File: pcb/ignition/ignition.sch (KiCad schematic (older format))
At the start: 174 parts, among them IC1 LTC4151, IC2 LTC4151, IC3 LTC4151, IC4 LTC4151, IC5 LTC4151, IC6 LTC4151, IC7 ADP3335, IC8 STM32F437VIT6, J1 PSU, J10 CH2, J11 CH4, J12 ARM, J13 UART1, J14 UART2, J15 CH1, J16 CH3, J17 CH5, J2 LED1, J3 PSU, J4 LED2, J5 5v In, J6 5v Out, J7 LED3, J8 LED4, J9 LED5, K1 16A SPST, K2 16A SPST, K3 16A SPST, K4 16A SPST, K5 16A SPST, K6 16A SPST, P1 SWD_TC, Q1 NFET, Q2 NFET, Q3 NFET, Q4 NFET, Q5 NFET, Q6 NFET, U1 MICROSD, X1 Molex Wire, X10 GRN LED, X11 LED Bezel, X12 24V PSU, X13 5V PSU, X14 GRN LED, X15 LED Bezel, X16 Molex Wire, X17 M12 Socket, X18 M12 Plug, X19 Molex Wire, X2 GRN LED, X20 M12 Socket, X21 M12 Plug, X22 Bi-LED, X23 LED Bezel, X24 Molex Wire, X25 M12 Socket, X26 M12 Plug, X27 Molex Wire, X28 M12 Socket, X29 M12 Plug, X3 LED Bezel, X30 Molex Wire, X31 M12 Socket, X32 M12 Plug, X33 Hole, X34 Hole, X35 Hole, X36 Hole, X4 GRN LED, X5 LED Bezel, X6 GRN LED, X7 LED Bezel, X8 Key Switch, X9 AC Input, Y1 26M

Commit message: ignition pcb almost complete
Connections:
- net ARM_GRN: now also IC8.51 (PB12); no longer IC8.39 (PE8)
- net ARM_RED: now also IC8.52 (PB13); no longer IC8.40 (PE9)
- net ARM_SUPPLY: now also IC8.1 (PE2); no longer IC8.55 (PD8)
- net CH1_FIRE: now also IC8.36 (PB1); no longer IC8.56 (PD9)
- net CH2_FIRE: now also IC8.37 (PB2); no longer IC8.57 (PD10)
- net CH3_FIRE: now also IC8.38 (PE7); no longer IC8.58 (PD11)
- net CH4_FIRE: now also IC8.39 (PE8); no longer IC8.59 (PD12)
- net CH5_FIRE: now also IC8.40 (PE9); no longer IC8.60 (PD13)
- net FIRE_DIST: now also D1.1, D2.1, D6.1, D7.1, D8.1, K1.2, K2.2, K4.2, K5.2, K6.2
- net PSU_MON: now also IC8.24 (PA1); no longer IC8.34 (PC5)
- net STATUS: now also IC8.64 (PC7); no longer IC8.43 (PE12)
- net VCC: now also D3.1, K3.2
- net at IC3.10 (SENSE-), K3.3, R13.1: no longer D3.1, K3.2
- net at IC4.10 (SENSE-), K4.3, R31.1: no longer D6.1, K4.2
- net at IC1.10 (SENSE-), K1.3, R7.1: no longer D1.1, K1.2
- net at IC5.10 (SENSE-), K5.3, R32.1: no longer D7.1, K5.2
- net at IC2.10 (SENSE-), K2.3, R8.1: no longer D2.1, K2.2
- net at IC6.10 (SENSE-), K6.3, R33.1: no longer D8.1, K6.2
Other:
- note added: "ADC12 IN 10-14"
- note removed: "ADC12 IN 10-15"
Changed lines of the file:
@@
 	1    0    0    -1
 $EndComp
-Wire Wire Line
-	3625 2600 3325 2600
 Connection ~ 2925 2600
 Wire Wire Line
 	3325 2750 3325 2850
 Wire Wire Line
-	3325 2750 3325 2600
-Connection ~ 3325 2750
-Connection ~ 3325 2600
-Wire Wire Line
-	3325 2600 2925 2600
-Wire Wire Line
 	1425 3675 1425 3400
 Connection ~ 1425 3400
@@
 Channel 1:
 Wire Wire Line
-	7975 2675 7975 2525
-Connection ~ 7975 2675
-Connection ~ 7975 2525
-Wire Wire Line
-	7975 2525 8275 2525
-Wire Wire Line
-	7600 2525 7975 2525
-Wire Wire Line
 	6100 2525 7300 2525
 Wire Wire Line
@@
 Channel 2:
 Wire Wire Line
-	3025 5225 3025 5075
-Connection ~ 3025 5225
-Connection ~ 3025 5075
-Wire Wire Line
-	3025 5075 3325 5075
-Wire Wire Line
-	2650 5075 3025 5075
-Wire Wire Line
 	1150 5075 2350 5075
 Wire Wire Line
@@
 Channel 3:
 Wire Wire Line
-	7975 5225 7975 5075
-Connection ~ 7975 5225
-Connection ~ 7975 5075
-Wire Wire Line
-	7975 5075 8275 5075
-Wire Wire Line
-	7600 5075 7975 5075
-Wire Wire Line
 	6100 5075 7300 5075
 Wire Wire Line
@@
 Channel 4:
 Wire Wire Line
-	3025 7725 3025 7575
-Connection ~ 3025 7725
-Connection ~ 3025 7575
-Wire Wire Line
-	3025 7575 3325 7575
-Wire Wire Line
-	2650 7575 3025 7575
-Wire Wire Line
 	1150 7575 2350 7575
 Wire Wire Line
@@
 Channel 5:
 Wire Wire Line
-	7975 7725 7975 7575
-Connection ~ 7975 7725
-Connection ~ 7975 7575
-Wire Wire Line
-	7975 7575 8275 7575
-Wire Wire Line
-	7600 7575 7975 7575
-Wire Wire Line
 	6100 7575 7300 7575
 Wire Wire Line
@@
 Wire Wire Line
 	2025 1075 2075 1075
-Text Label 14125 5725 0    50   ~ 0
+Text Label 12725 6825 2    50   ~ 0
 ARM_GRN
-Text Label 14125 5825 0    50   ~ 0
+Text Label 12725 6925 2    50   ~ 0
 ARM_RED
 Text Label 14125 1225 0    50   ~ 0
@@
 Text Label 14125 1325 0    50   ~ 0
 CH2_CONT
-Text Label 14125 1725 0    50   ~ 0
+Text Label 12725 3825 2    50   ~ 0
 PSU_MON
-Text Label 14125 3925 0    50   ~ 0
+Text Label 14125 5025 0    50   ~ 0
 ARM_SUPPLY
-Text Label 14125 4125 0    50   ~ 0
+Text Label 12725 5725 2    50   ~ 0
 CH2_FIRE
-Text Label 14125 4025 0    50   ~ 0
+Text Label 12725 5625 2    50   ~ 0
 CH1_FIRE
-Text Label 14125 4225 0    50   ~ 0
+Text Label 14125 5525 0    50   ~ 0
 CH3_FIRE
-Text Label 14125 4325 0    50   ~ 0
+Text Label 14125 5725 0    50   ~ 0
 CH4_FIRE
-Text Label 14125 4425 0    50   ~ 0
+Text Label 14125 5825 0    50   ~ 0
 CH5_FIRE
 Text Label 12725 6725 2    50   ~ 0
@@
 	1    0    0    -1
 $EndComp
-Text Label 14125 6125 0    50   ~ 0
+Text Label 14125 1925 0    50   ~ 0
 STATUS
 $Comp
@@
 	14025 1625 14125 1625
 Wire Wire Line
-	14025 1725 14125 1725
+	12825 3825 12725 3825
 NoConn ~ 14025 1825
-NoConn ~ 14025 1925
 Text Notes 14700 1450 0    50   ~ 0
-ADC12 IN 10-15
+ADC12 IN 10-14
 Wire Wire Line
 	12725 6425 12825 6425
@@
 USART2_RX
 Wire Wire Line
-	14025 3925 14125 3925
+	14025 5025 14125 5025
 Wire Wire Line
-	14125 4025 14025 4025
+	12725 5625 12825 5625
 Wire Wire Line
-	14025 4125 14125 4125
+	12825 5725 12725 5725
 Wire Wire Line
-	14025 4225 14125 4225
+	14025 5525 14125 5525
 Wire Wire Line
-	14025 4325 14125 4325
+	14025 5725 14125 5725
 Wire Wire Line
-	14025 4425 14125 4425
+	14025 5825 14125 5825
 Wire Wire Line
-	14025 5725 14125 5725
+	12825 6825 12725 6825
 Wire Wire Line
-	14125 5825 14025 5825
+	12725 6925 12825 6925
 Wire Wire Line
-	14025 6125 14125 6125
+	14025 1925 14125 1925
 NoConn ~ 14025 6425
 NoConn ~ 14025 6325
 NoConn ~ 14025 6225
 NoConn ~ 14025 6025
-NoConn ~ 14025 5925
-NoConn ~ 14025 5525
 NoConn ~ 14025 5425
 NoConn ~ 14025 5325
 NoConn ~ 14025 5225
 NoConn ~ 14025 5125
-NoConn ~ 14025 5025
 NoConn ~ 14025 4925
 NoConn ~ 14025 4825
@@
 NoConn ~ 12825 7125
 NoConn ~ 12825 7025
-NoConn ~ 12825 6925
-NoConn ~ 12825 6825
 NoConn ~ 12825 6225
 NoConn ~ 12825 6125
-NoConn ~ 12825 5525
-NoConn ~ 12825 5625
-NoConn ~ 12825 5725
 NoConn ~ 12825 5825
 NoConn ~ 12825 5925
@@
 NoConn ~ 12825 4225
 NoConn ~ 12825 4125
-NoConn ~ 12825 3825
 NoConn ~ 12825 3725
 NoConn ~ 14025 3725
@@
 	1    0    0    -1
 $EndComp
+Text Label 7975 2675 2    50   ~ 0
+FIRE_DIST
+Wire Wire Line
+	7600 2525 8275 2525
+Text Label 7975 5225 2    50   ~ 0
+FIRE_DIST
+Wire Wire Line
+	7600 5075 8275 5075
+Text Label 3025 5225 2    50   ~ 0
+FIRE_DIST
+Wire Wire Line
+	2650 5075 3325 5075
+Text Label 3025 7725 2    50   ~ 0
+FIRE_DIST
+Wire Wire Line
+	2650 7575 3325 7575
+Text Label 7975 7725 2    50   ~ 0
+FIRE_DIST
+Wire Wire Line
+	7600 7575 8275 7575
+NoConn ~ 12825 5525
+NoConn ~ 14025 4025
+NoConn ~ 14025 4125
+NoConn ~ 14025 4225
+NoConn ~ 14025 4325
+NoConn ~ 14025 4425
+NoConn ~ 14025 6125
+NoConn ~ 14025 3925
+NoConn ~ 14025 5925
+NoConn ~ 14025 1725
+$Comp
+L voltages:24v #PWR?
+U 1 1 5CA17557
+P 3250 2750
+F 0 "#PWR?" H 3250 2860 50  0001 L CNN
+F 1 "24v" H 3250 2850 50  0000 C CNN
+F 2 "" H 3250 2750 50  0001 C CNN
+F 3 "" H 3250 2750 50  0001 C CNN
+	1    3250 2750
+	0    -1   -1   0
+$EndComp
+Wire Wire Line
+	2925 2600 3625 2600
+Wire Wire Line
+	3250 2750 3325 2750
+Connection ~ 3325 2750
 $EndSCHEMATC

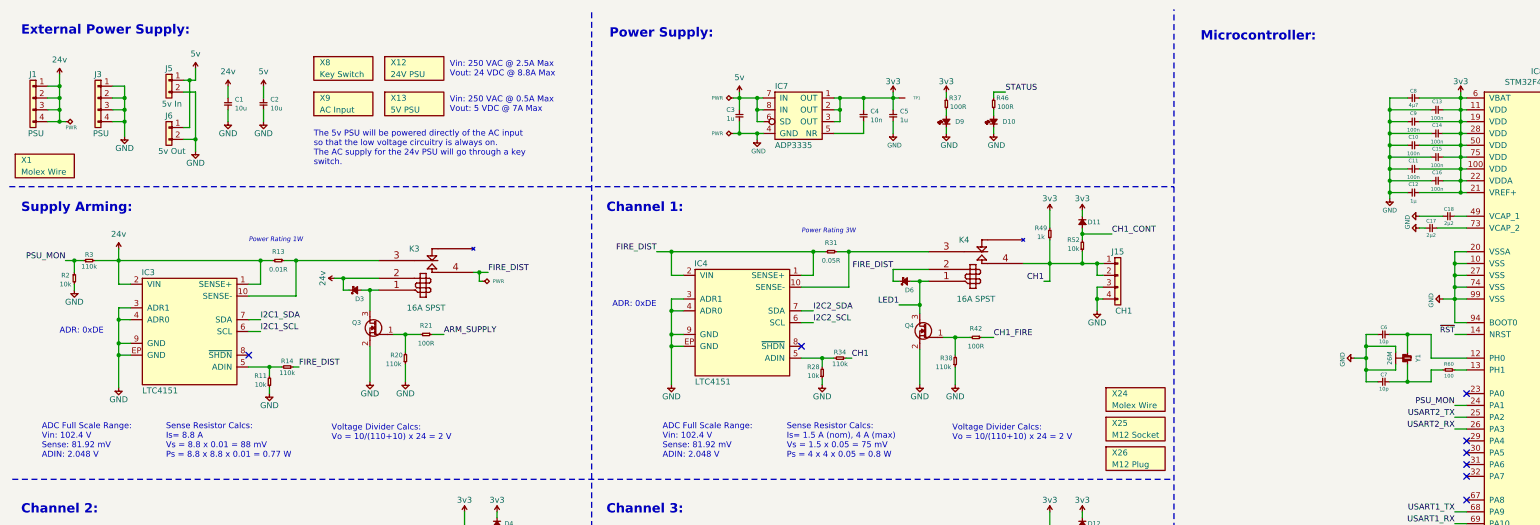
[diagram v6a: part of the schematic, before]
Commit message: finalised schematic and pcb copper, adding silk
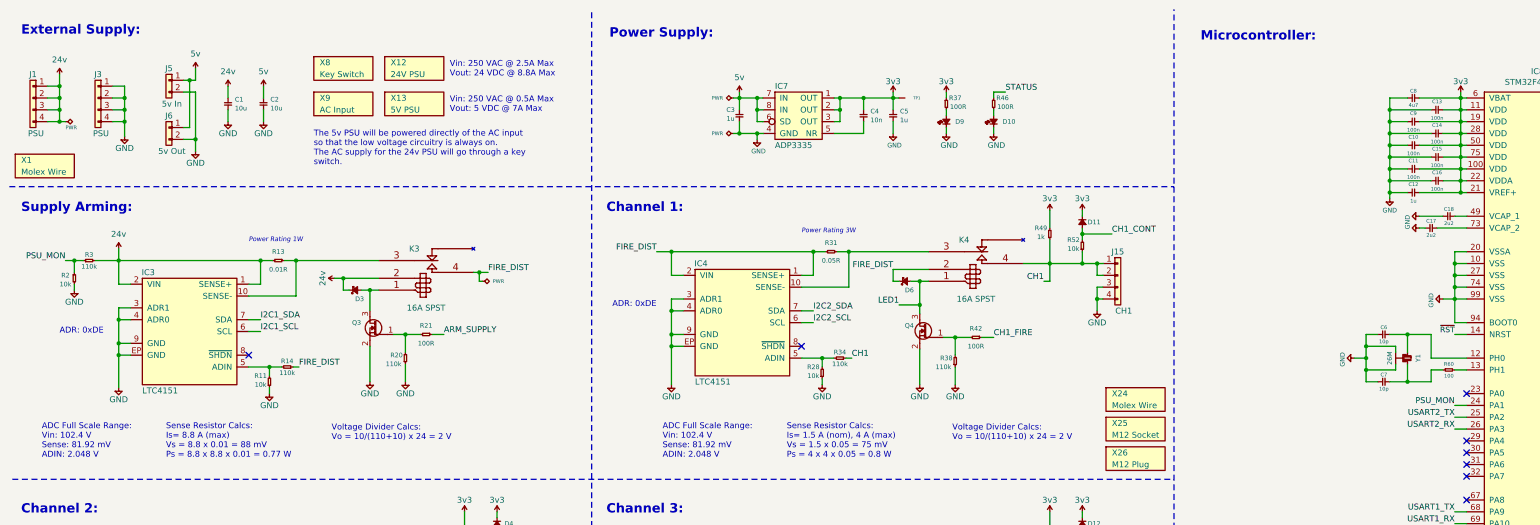
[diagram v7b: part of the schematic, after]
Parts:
- C12: value 1µ -> 1u
- C17, C18: value 2µ2 -> 2u2
- C8: value 4µ7 -> 4u7
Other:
- note added: "External Supply:"
- note added: "Sense Resistor Calcs:\nIs= 8.8 A (max)\nVs = 8.8 x 0.01 = 88 mV\nPs = 8.8 x 8.8 x 0.01 = 0.77 W"
- note removed: "External Power Supply:"
- note removed: "Sense Resistor Calcs:\nIs= 8.8 A\nVs = 8.8 x 0.01 = 88 mV\nPs = 8.8 x 8.8 x 0.01 = 0.77 W"
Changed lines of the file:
@@
 encoding utf-8
 Sheet 1 1
-Title "Valve Controller"
-Date "2018-11-03"
+Title "Ignition Board"
+Date "2018-11-11"
 Rev "1"
-Comp "Matt Coates"
-Comment1 ""
+Comp "Matthew Coates"
+Comment1 "Hybrid Ignition Controller"
 Comment2 ""
 Comment3 ""
@@
 $EndComp
 Text Notes 600  700  0    79   ~ 16
-External Power Supply:
+External Supply:
 Wire Wire Line
 	1425 2800 1525 2800
@@
 Power Rating 1W
 Text Notes 1825 4275 0    50   ~ 0
-Sense Resistor Calcs:\nIs= 8.8 A\nVs = 8.8 x 0.01 = 88 mV\nPs = 8.8 x 8.8 x 0.01 = 0.77 W
+Sense Resistor Calcs:\nIs= 8.8 A (max)\nVs = 8.8 x 0.01 = 88 mV\nPs = 8.8 x 8.8 x 0.01 = 0.77 W
 Text Notes 3225 4125 0    50   ~ 0
 Voltage Divider Calcs:\nVo = 10/(110+10) x 24 = 2 V
@@
 P 12725 2225
 F 0 "C18" H 12775 2165 31  0000 C CNN
-F 1 "2µ2" H 12775 2285 31  0000 C CNN
+F 1 "2u2" H 12775 2285 31  0000 C CNN
 F 2 "agg:0402" H 12725 2225 50  0001 C CNN
 F 3 "" H 12725 2225 50  0001 C CNN
@@
 P 12575 2325
 F 0 "C17" H 12625 2265 31  0000 C CNN
-F 1 "2µ2" H 12625 2385 31  0000 C CNN
+F 1 "2u2" H 12625 2385 31  0000 C CNN
 F 2 "agg:0402" H 12575 2325 50  0001 C CNN
 F 3 "" H 12575 2325 50  0001 C CNN
@@
 P 12325 2025
 F 0 "C12" H 12375 2095 31  0000 C CNN
-F 1 "1µ" H 12375 1955 31  0000 C CNN
+F 1 "1u" H 12375 1955 31  0000 C CNN
 F 2 "agg:0402" H 12325 2025 50  0001 C CNN
 F 3 "" H 12325 2025 50  0001 C CNN
@@
 P 12325 1225
 F 0 "C8" H 12375 1285 31  0000 C CNN
-F 1 "4µ7" H 12375 1165 31  0000 C CNN
+F 1 "4u7" H 12375 1165 31  0000 C CNN
 F 2 "agg:0402" H 12325 1225 50  0001 C CNN
 F 3 "" H 12325 1225 50  0001 C CNN
@@
 NoConn ~ 14025 1725
 $Comp
-L voltages:24v #PWR?
+L voltages:24v #PWR0101
 U 1 1 5CA17557
 P 3250 2750
-F 0 "#PWR?" H 3250 2860 50  0001 L CNN
+F 0 "#PWR0101" H 3250 2860 50  0001 L CNN
 F 1 "24v" H 3250 2850 50  0000 C CNN
 F 2 "" H 3250 2750 50  0001 C CNN

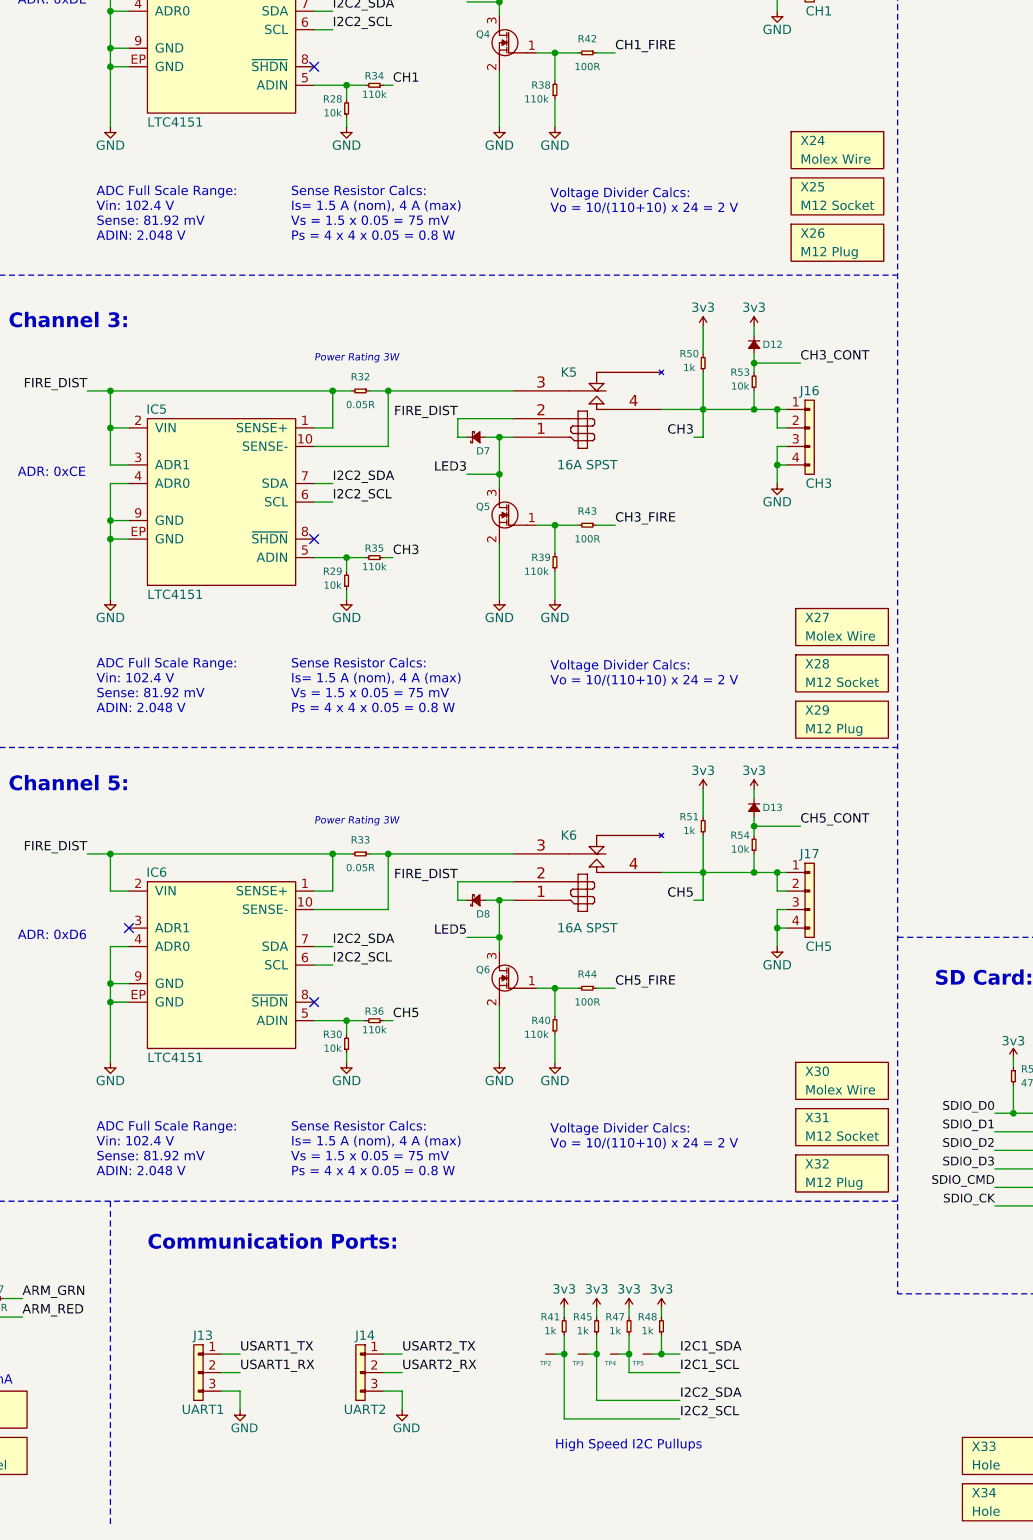
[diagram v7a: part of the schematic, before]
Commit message: made changes to ignition as per review
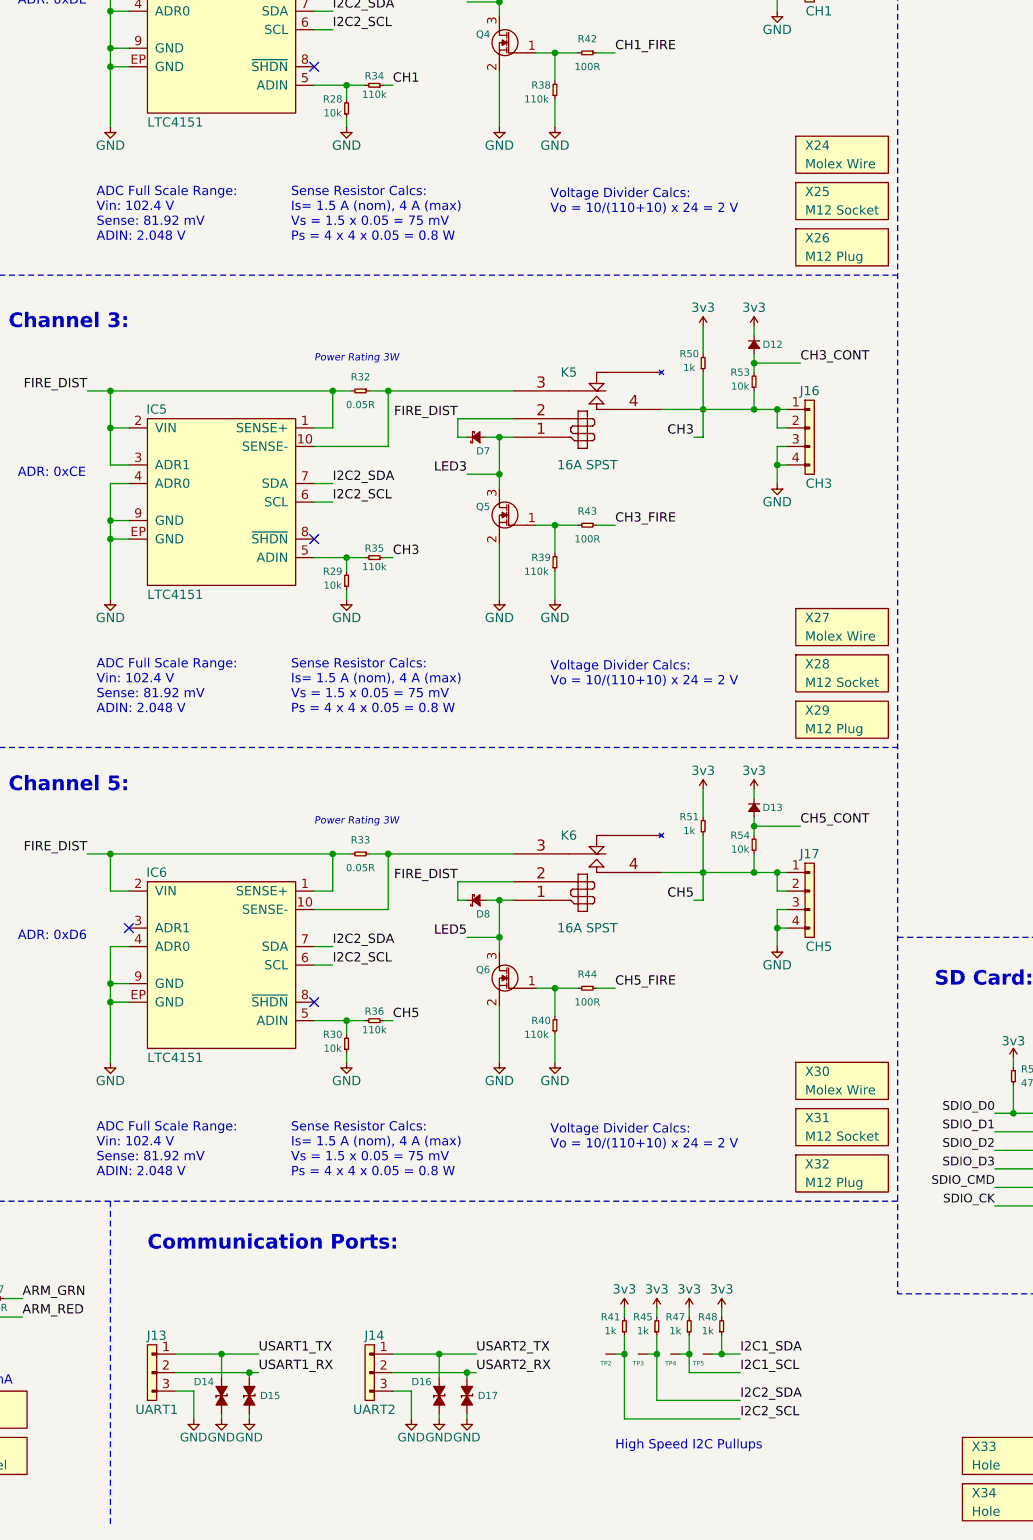
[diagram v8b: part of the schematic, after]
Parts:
- added D14, D15, D16, D17: ESD_DIODE, agg:0402, symbol agg-kicad:ESD_DIODE
- X17, X20, X25, X28, X31: Farnell 2627740 -> 2723662
- X18, X21, X26, X29, X32: Farnell 2723656 -> 2627737
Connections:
- net GND: now also D14.2, D15.2, D16.2, D17.2
- net USART1_RX: now also D15.1
- net USART1_TX: now also D14.1
- net USART2_RX: now also D17.1
- net USART2_TX: now also D16.1
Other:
- moved on the sheet: J13, R41, R45, R47, R48, TP2, TP3, TP4, TP5
